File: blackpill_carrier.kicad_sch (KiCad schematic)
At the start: 33 parts, among them J1 Conn_01x03, J2 FTSH-105-01-F-DV-K-P-TR, J3 Conn_ARM_JTAG_SWD_10, J4 PicoBlade, U1 Blackpill F411

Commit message: Partial BOM updates for LCSC part numbers
The Picoblade and the Blackpill need addressing. For the Blackpill, need to switch to using a set of SMT headers (to reduce assembly cost).
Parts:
- D1: LCSC (none) -> C94868
- D2, D4: LCSC (none) -> C98221
- D3: LCSC (none) -> C98222
- J1: LCSC (none) -> C5967212
- J2: LCSC (none) -> C5250218
- J3: value Conn_ARM_JTAG_SWD_10 -> FTSH-105-01-F-DV-K-P-TR; LCSC (none) -> C5250218
- R1, R2: LCSC (none) -> C25201
- R3, R4, R5, R6: LCSC (none) -> C25585
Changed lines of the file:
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@@
       (effects (font (size 1.27 1.27)) (justify right))
     )
-    (property "Value" "Conn_ARM_JTAG_SWD_10" (at 35.56 140.335 0)
+    (property "Value" "FTSH-105-01-F-DV-K-P-TR" (at 35.56 140.335 0)
       (effects (font (size 1.27 1.27)) (justify right) hide)
     )
@@
     )
     (property "Mouser" "200-FTSH10501FDVKPTR" (at 47.625 139.065 0)
+      (effects (font (size 1.27 1.27)) hide)
+    )
+    (property "LCSC" "C5250218" (at 47.625 139.065 0)
       (effects (font (size 1.27 1.27)) hide)
     )
@@
       (effects (font (size 1.27 1.27)) hide)
     )
+    (property "LCSC" "C98222" (at 239.395 82.55 0)
+      (effects (font (size 1.27 1.27)) hide)
+    )
     (pin "1")
     (pin "2")
@@
       (effects (font (size 1.27 1.27)) hide)
     )
+    (property "LCSC" "C25201" (at 221.615 42.545 0)
+      (effects (font (size 1.27 1.27)) hide)
+    )
     (pin "1")
     (pin "2")
@@
     )
     (property "Datasheet" "~" (at 230.505 95.25 0)
+      (effects (font (size 1.27 1.27)) hide)
+    )
+    (property "LCSC" "C25585" (at 230.505 95.25 0)
       (effects (font (size 1.27 1.27)) hide)
     )
@@
       (effects (font (size 1.27 1.27)) hide)
     )
+    (property "LCSC" "C5250218" (at 47.625 66.04 0)
+      (effects (font (size 1.27 1.27)) hide)
+    )
     (pin "1")
     (pin "10")
@@
       (effects (font (size 1.27 1.27)) hide)
     )
+    (property "LCSC" "C25201" (at 221.615 45.085 0)
+      (effects (font (size 1.27 1.27)) hide)
+    )
     (pin "1")
     (pin "2")
@@
       (effects (font (size 1.27 1.27)) hide)
     )
+    (property "LCSC" "C98221" (at 239.395 100.965 0)
+      (effects (font (size 1.27 1.27)) hide)
+    )
     (pin "1")
     (pin "2")
@@
       (effects (font (size 1.27 1.27)) hide)
     )
+    (property "LCSC" "C25585" (at 230.505 100.965 0)
+      (effects (font (size 1.27 1.27)) hide)
+    )
     (pin "1")
     (pin "2")
@@
       (effects (font (size 1.27 1.27)) hide)
     )
+    (property "LCSC" "C98221" (at 239.395 106.68 0)
+      (effects (font (size 1.27 1.27)) hide)
+    )
     (pin "1")
     (pin "2")
@@
     )
     (property "Datasheet" "~" (at 239.395 95.25 90)
+      (effects (font (size 1.27 1.27)) hide)
+    )
+    (property "LCSC" "C94868" (at 239.395 95.25 0)
       (effects (font (size 1.27 1.27)) hide)
     )
@@
       (effects (font (size 1.27 1.27)) hide)
     )
+    (property "LCSC" "C5967212" (at 47.625 38.735 90)
+      (effects (font (size 1.27 1.27)) hide)
+    )
     (pin "1")
     (pin "2")
@@
       (effects (font (size 1.27 1.27)) hide)
     )
+    (property "LCSC" "C25585" (at 230.505 82.55 0)
+      (effects (font (size 1.27 1.27)) hide)
+    )
     (pin "1")
     (pin "2")
@@
       (effects (font (size 1.27 1.27)) hide)
     )
+    (property "LCSC" "C25585" (at 230.505 106.68 0)
+      (effects (font (size 1.27 1.27)) hide)
+    )

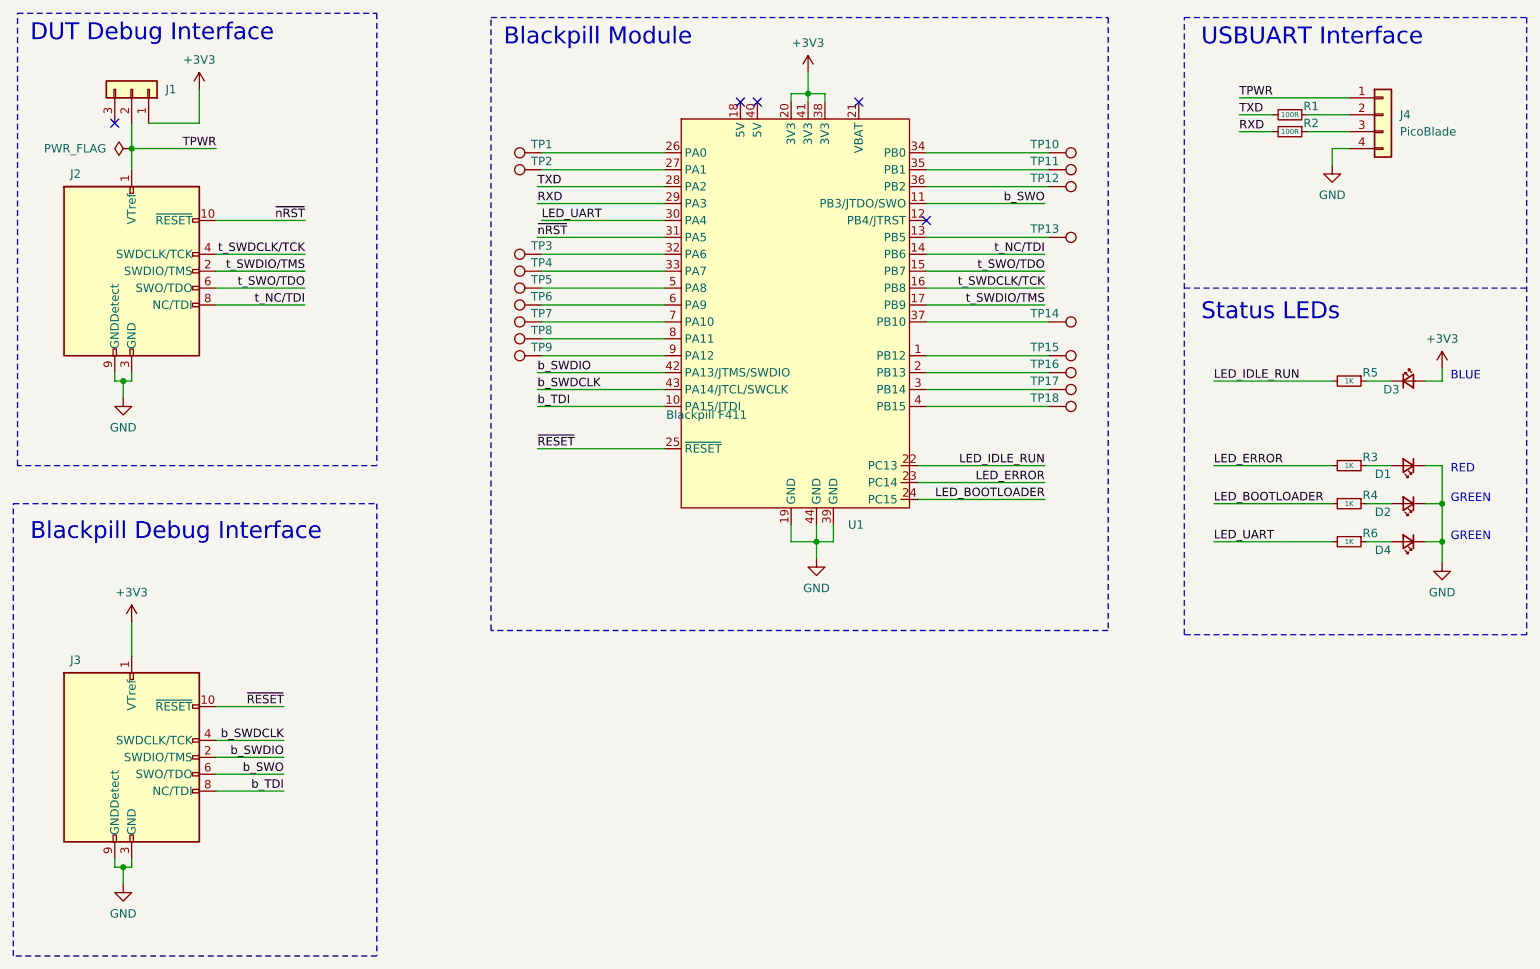
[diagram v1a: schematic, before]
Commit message: Initial layout and component updates
May require more work after testing is completed
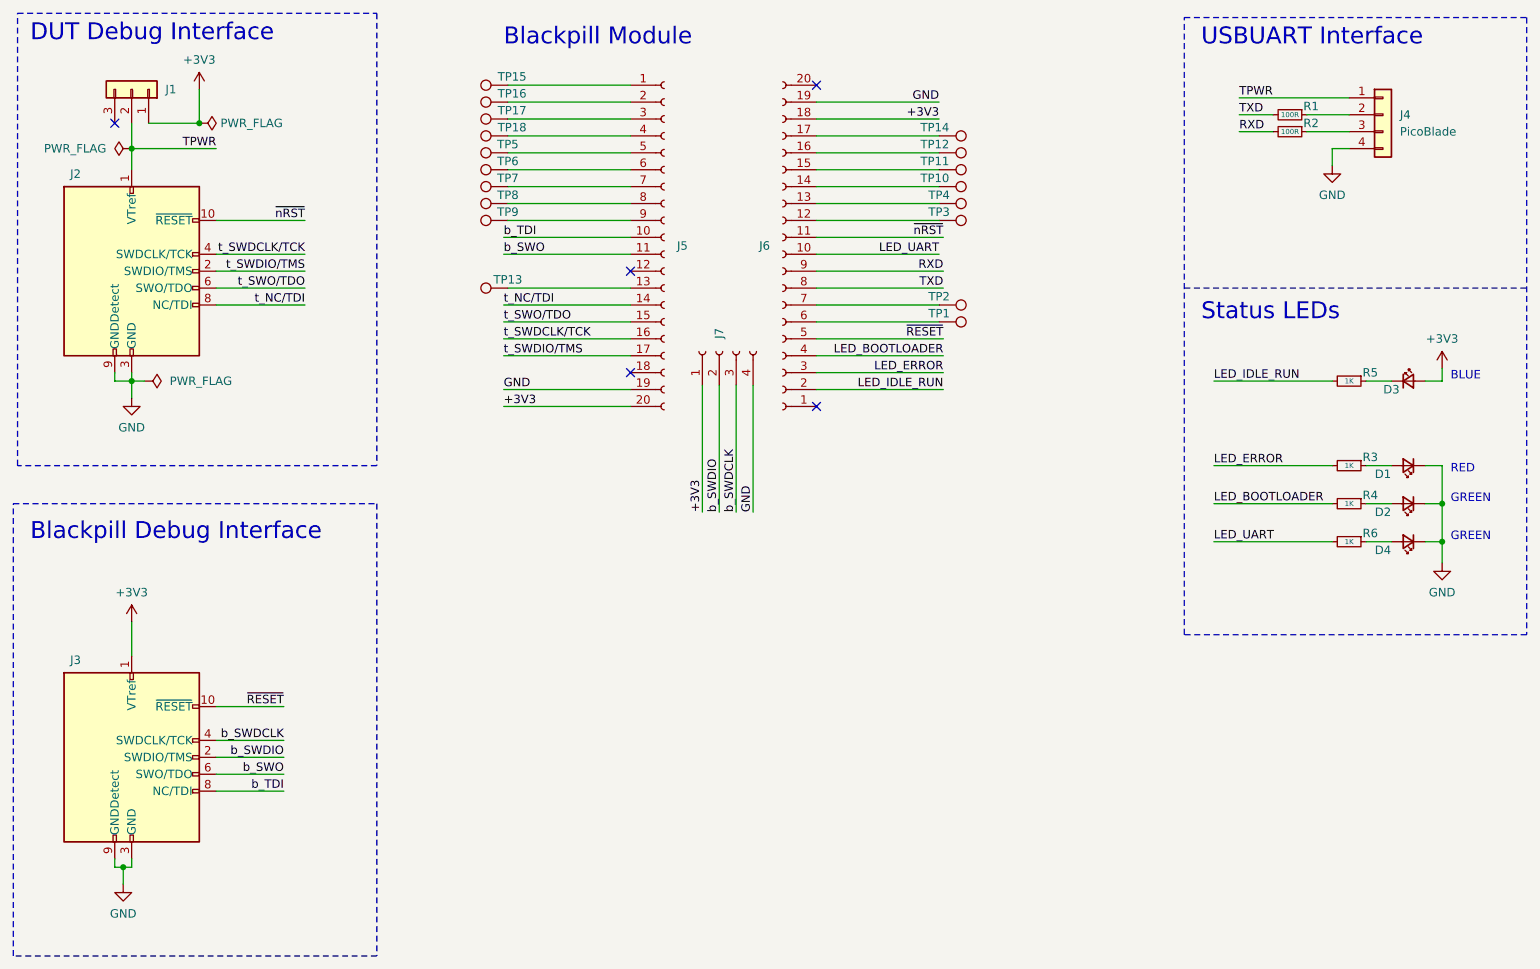
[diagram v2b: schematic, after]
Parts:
- removed U1: Blackpill F411, sjp_modules:Blackpill F411, symbol sjp_modules:Blackpill_F411
- added J5, J6: Conn_01x40_Socket, Connector_PinSocket_2.54mm:PinSocket_1x20_P2.54mm_Vertical, symbol Connector:Conn_01x20_Socket
- added J7: Conn_01x04_Socket, Connector_PinSocket_2.54mm:PinSocket_1x04_P2.54mm_Vertical, symbol Connector:Conn_01x04_Socket
- J1: footprint PinHeader_1x03_P1.00mm_Vertical_SMD_Pin1Right -> Connector_PinHeader_2.54mm:PinHeader_1x03_P2.54mm_Vertical_SMD_Pin1Right
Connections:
- net +3V3: now also J5.20 (Pin_20), J6.18 (Pin_18), J7.1 (Pin_1)
- net GND: now also J5.19 (Pin_19), J6.19 (Pin_19), J7.4 (Pin_4)
- net LED_BOOTLOADER: now also J6.4 (Pin_4)
- net LED_ERROR: now also J6.3 (Pin_3)
- net LED_IDLE_RUN: now also J6.2 (Pin_2)
- net LED_UART: now also J6.10 (Pin_10)
- net RXD: now also J6.9 (Pin_9)
- net TXD: now also J6.8 (Pin_8)
- net b_SWDCLK: now also J7.3 (Pin_3)
- net b_SWDIO: now also J7.2 (Pin_2)
- net b_SWO: now also J5.11 (Pin_11)
- net b_TDI: now also J5.10 (Pin_10)
- net t_NC/TDI: now also J5.14 (Pin_14)
- net t_SWDCLK/TCK: now also J5.16 (Pin_16)
- net t_SWDIO/TMS: now also J5.17 (Pin_17)
- net t_SWO/TDO: now also J5.15 (Pin_15)
- net ~{RESET}: now also J6.5 (Pin_5)
- net ~{nRST}: now also J6.11 (Pin_11)
- net at TP10.1: now also J6.14 (Pin_14)
- net at TP3.1: now also J6.12 (Pin_12)
- net at TP17.1: now also J5.3 (Pin_3)
- net at TP15.1: now also J5.1 (Pin_1)
- net at TP13.1: now also J5.13 (Pin_13)
- net at TP16.1: now also J5.2 (Pin_2)
- net at TP1.1: now also J6.6 (Pin_6)
- net at TP2.1: now also J6.7 (Pin_7)
- net at TP4.1: now also J6.13 (Pin_13)
- net at TP11.1: now also J6.15 (Pin_15)
- net at TP12.1: now also J6.16 (Pin_16)
- net at TP14.1: now also J6.17 (Pin_17)
- net at TP18.1: now also J5.4 (Pin_4)
- net at TP5.1: now also J5.5 (Pin_5)
- net at TP6.1: now also J5.6 (Pin_6)
- net at TP7.1: now also J5.7 (Pin_7)
- net at TP8.1: now also J5.8 (Pin_8)
- net at TP9.1: now also J5.9 (Pin_9)
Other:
- moved on the sheet: TP1, TP10, TP11, TP12, TP13, TP14, TP15, TP16, TP17, TP18, TP2, TP3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

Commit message: Remove test points etc.
Removed all components not REQUIRED for BMF to operate.
Also removed unwanted jumper.
Changed footprint of target power selector.
Added pull-down for PA10
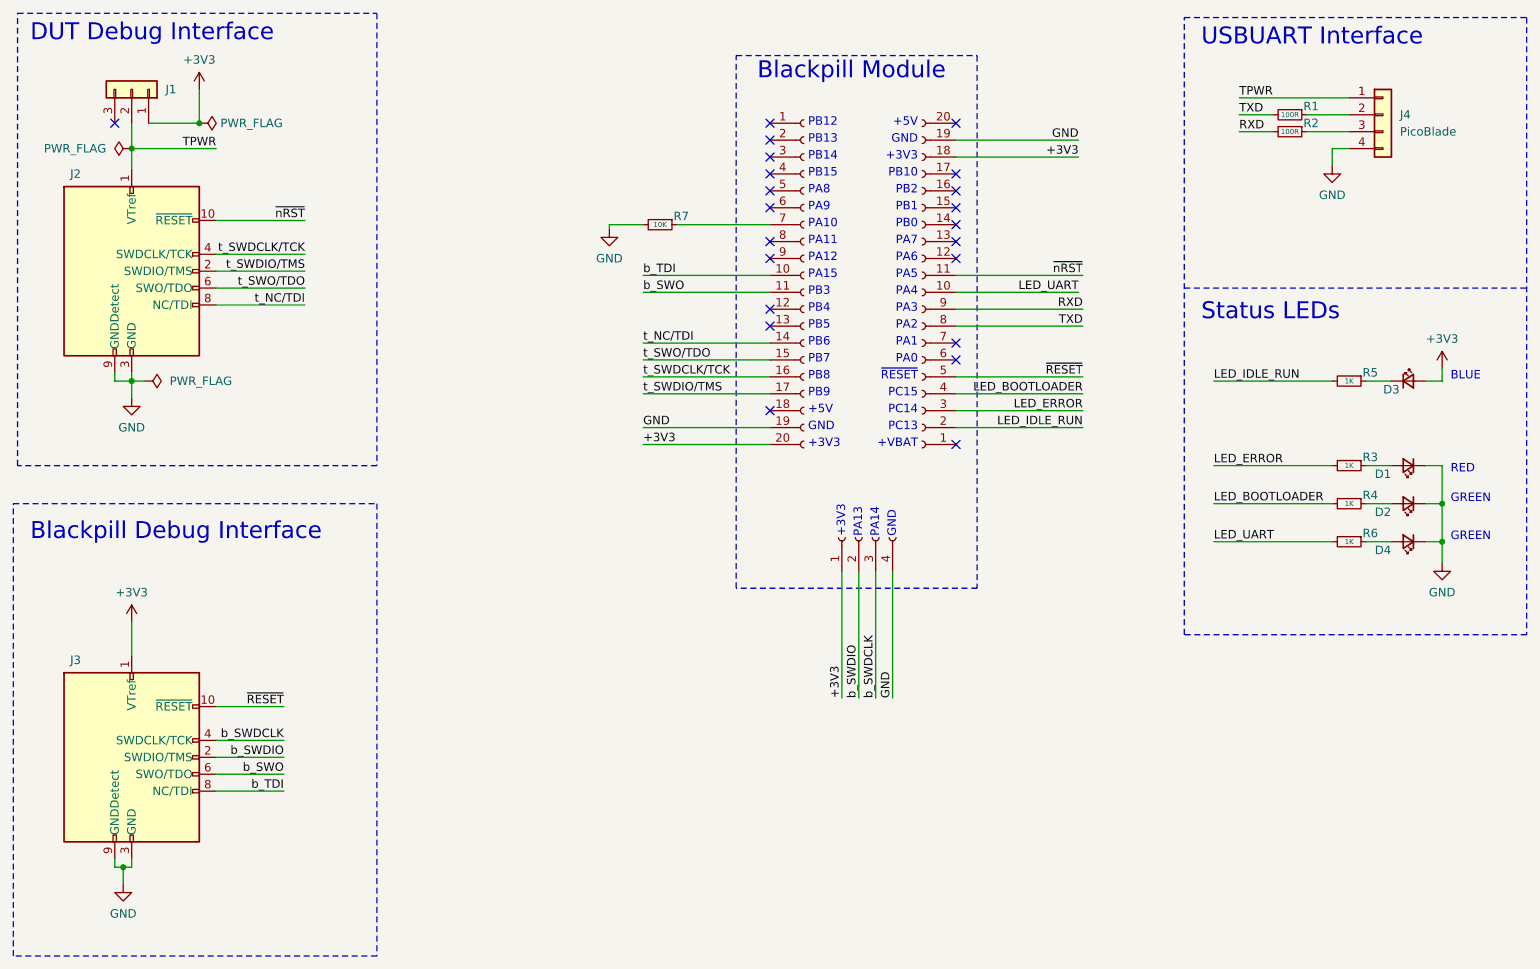
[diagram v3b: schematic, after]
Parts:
- removed TP1, TP10, TP11, TP12, TP13, TP14, TP15, TP16, TP17, TP18, TP2, TP3, TP4, TP5, TP6, TP7, TP8, TP9: TestPoint, sjp_connectors:151-201-RC-Testpoint, symbol Connector:TestPoint
- added R7: 10K, Resistor_SMD:R_0603_1608Metric, symbol Device:R_Small
- J1: value Conn_01x03 -> M50-3630342; footprint Connector_PinHeader_2.54mm:PinHeader_1x03_P2.54mm_Vertical_SMD_Pin1Right -> Connector_PinHeader_1.27mm:PinHeader_1x03_P1.27mm_Vertical_SMD_Pin1Right; LCSC C5967212 -> C3336318; Mouser (none) -> 855-M50-3630342
- J4: LCSC (none) -> C17617036
- J5, J6: value Conn_01x40_Socket -> B-2200S20P-A120; LCSC (none) -> C124410
- J7: value Conn_01x04_Socket -> B-2200S04P-A120; LCSC (none) -> C124413
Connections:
- net GND: now also R7.2
- net at J5.7 (Pin_7): now also R7.1
- no-connect marks 5 -> 22
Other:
- note added: "+3V3"
- note added: "+5V"
- note added: "+VBAT"
- note added: "GND"
- note added: "PA0"
- note added: "PA1"
- note added: "PA10"
- note added: "PA11"
- note added: "PA12"
- note added: "PA13"
- note added: "PA14"
- note added: "PA15"
- note added: "PA2"
- note added: "PA3"
- note added: "PA4"
- note added: "PA5"
- note added: "PA6"
- note added: "PA7"
- note added: "PA8"
- note added: "PA9"
- note added: "PB0"
- note added: "PB1"
- note added: "PB10"
- note added: "PB12"
- note added: "PB13"
- note added: "PB14"
- note added: "PB15"
- note added: "PB2"
- note added: "PB3"
- note added: "PB4"
- note added: "PB5"
- note added: "PB6"
- note added: "PB7"
- note added: "PB8"
- note added: "PB9"
- note added: "PC13"
- note added: "PC14"
- note added: "PC15"
- note added: "~{RESET}"

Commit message: Updates for PCBWay
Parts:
- D1: MPN (none) -> LTSTC170KR
- D2, D4: MPN (none) -> LTSTC170KG
- D3: MPN (none) -> LTSTC170KB
- J1: MPN (none) -> M50-3630342
- J2, J3: footprint Connector_PinHeader_1.27mm:PinHeader_2x05_P1.27mm_Vertical_SMD -> sjp_connectors:FTSH-105-XX-X-DV; MPN (none) -> FTSH-105-01-F-DV-K-P-TR
- J4: MPN (none) -> 53261-0471
- J5, J6: MPN (none) -> 6-534237-8
- J7: MPN (none) -> 215299-4
- R1, R2: MPN (none) -> ERJ-3GEYJ101V
- R3, R4, R5, R6: MPN (none) -> ERJ-U03J102V
- R7: MPN (none) -> ERJ-3GEYJ103V
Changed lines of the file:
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@@
       (effects (font (size 1.27 1.27)) (justify right) hide)
     )
-    (property "Footprint" "Connector_PinHeader_1.27mm:PinHeader_2x05_P1.27mm_Vertical_SMD" (at 47.625 139.065 0)
+    (property "Footprint" "sjp_connectors:FTSH-105-XX-X-DV" (at 47.625 139.065 0)
       (effects (font (size 1.27 1.27)) hide)
     )
@@
     )
     (property "LCSC" "C5250218" (at 47.625 139.065 0)
+      (effects (font (size 1.27 1.27)) hide)
+    )
+    (property "MPN" "FTSH-105-01-F-DV-K-P-TR" (at 47.625 139.065 0)
       (effects (font (size 1.27 1.27)) hide)
     )
@@
       (effects (font (size 1.27 1.27)) hide)
     )
+    (property "MPN" "LTSTC170KB" (at 239.395 82.55 0)
+      (effects (font (size 1.27 1.27)) hide)
+    )
     (pin "1")
     (pin "2")
@@
       (effects (font (size 1.27 1.27)) hide)
     )
+    (property "MPN" "ERJ-3GEYJ101V" (at 221.615 42.545 0)
+      (effects (font (size 1.27 1.27)) hide)
+    )
     (pin "1")
     (pin "2")
@@
       (effects (font (size 1.27 1.27)) hide)
     )
+    (property "MPN" "ERJ-U03J102V" (at 230.505 95.25 0)
+      (effects (font (size 1.27 1.27)) hide)
+    )
     (pin "1")
     (pin "2")
@@
       (effects (font (size 1.27 1.27)) (justify right) hide)
     )
-    (property "Footprint" "Connector_PinHeader_1.27mm:PinHeader_2x05_P1.27mm_Vertical_SMD" (at 47.625 66.04 0)
+    (property "Footprint" "sjp_connectors:FTSH-105-XX-X-DV" (at 47.625 66.04 0)
       (effects (font (size 1.27 1.27)) hide)
     )
@@
     )
     (property "LCSC" "C5250218" (at 47.625 66.04 0)
+      (effects (font (size 1.27 1.27)) hide)
+    )
+    (property "MPN" "FTSH-105-01-F-DV-K-P-TR" (at 47.625 66.04 0)
       (effects (font (size 1.27 1.27)) hide)
     )
@@
       (effects (font (size 1.27 1.27)) hide)
     )
+    (property "MPN" "ERJ-3GEYJ101V" (at 221.615 45.085 0)
+      (effects (font (size 1.27 1.27)) hide)
+    )
     (pin "1")
     (pin "2")
@@
       (effects (font (size 1.27 1.27)) hide)
     )
+    (property "MPN" "53261-0471" (at 235.585 42.545 0)
+      (effects (font (size 1.27 1.27)) hide)
+    )
     (pin "1")
     (pin "2")
@@
       (effects (font (size 1.27 1.27)) hide)
     )
+    (property "MPN" "215299-4" (at 156.845 106.045 0)
+      (effects (font (size 1.27 1.27)) hide)
+    )
     (pin "1")
     (pin "2")
@@
       (effects (font (size 1.27 1.27)) hide)
     )
+    (property "MPN" "LTSTC170KG" (at 239.395 100.965 0)
+      (effects (font (size 1.27 1.27)) hide)
+    )
     (pin "1")
     (pin "2")
@@
       (effects (font (size 1.27 1.27)) hide)
     )
+    (property "MPN" "ERJ-U03J102V" (at 230.505 100.965 0)
+      (effects (font (size 1.27 1.27)) hide)
+    )
     (pin "1")
     (pin "2")
@@
       (effects (font (size 1.27 1.27)) hide)
     )
+    (property "MPN" "LTSTC170KG" (at 239.395 106.68 0)
+      (effects (font (size 1.27 1.27)) hide)
+    )
     (pin "1")
     (pin "2")
@@
     )
     (property "LCSC" "C124410" (at 166.37 69.215 0)
+      (effects (font (size 1.27 1.27)) hide)
+    )
+    (property "MPN" "6-534237-8" (at 166.37 69.215 0)
       (effects (font (size 1.27 1.27)) hide)
     )
@@
       (effects (font (size 1.27 1.27)) hide)
     )
+    (property "MPN" "6-534237-8" (at 148.59 66.675 0)
+      (effects (font (size 1.27 1.27)) hide)
+    )
     (pin "1")
     (pin "10")
@@
       (effects (font (size 1.27 1.27)) hide)
     )
+    (property "MPN" "LTSTC170KR" (at 239.395 95.25 0)
+      (effects (font (size 1.27 1.27)) hide)
+    )
     (pin "1")
     (pin "2")
@@
       (effects (font (size 1.27 1.27)) hide)
     )
+    (property "MPN" "M50-3630342" (at 47.625 38.735 0)
+      (effects (font (size 1.27 1.27)) hide)
+    )
     (pin "1")
     (pin "2")
@@
       (effects (font (size 1.27 1.27)) hide)
     )
+    (property "MPN" "ERJ-U03J102V" (at 230.505 82.55 0)
+      (effects (font (size 1.27 1.27)) hide)
+    )
     (pin "1")
     (pin "2")
@@
       (effects (font (size 1.27 1.27)) hide)
     )
+    (property "MPN" "ERJ-U03J102V" (at 230.505 106.68 0)
+      (effects (font (size 1.27 1.27)) hide)
+    )
     (pin "1")
     (pin "2")
@@
       (effects (font (size 1.27 1.27)) hide)
     )
+    (property "MPN" "ERJ-3GEYJ103V" (at 127 59.055 0)
+      (effects (font (size 1.27 1.27)) hide)
+    )
